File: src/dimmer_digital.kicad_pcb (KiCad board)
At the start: 2 copper layers, 82.5 x 55.9 mm, 28 parts, among them J2 CONECTOR_LEFT, J3 CONNECTOR_SPEED, J4 TERMINAL_AC, J5 TERMINAL_LOAD, J6 CONECTOR_RIGHT, Q1 TIC226, SW1 SWITCH_SPEED, SW2 SW_Push, U1 ATtiny13A-PU, U2 MOC3021M, U3 4N25

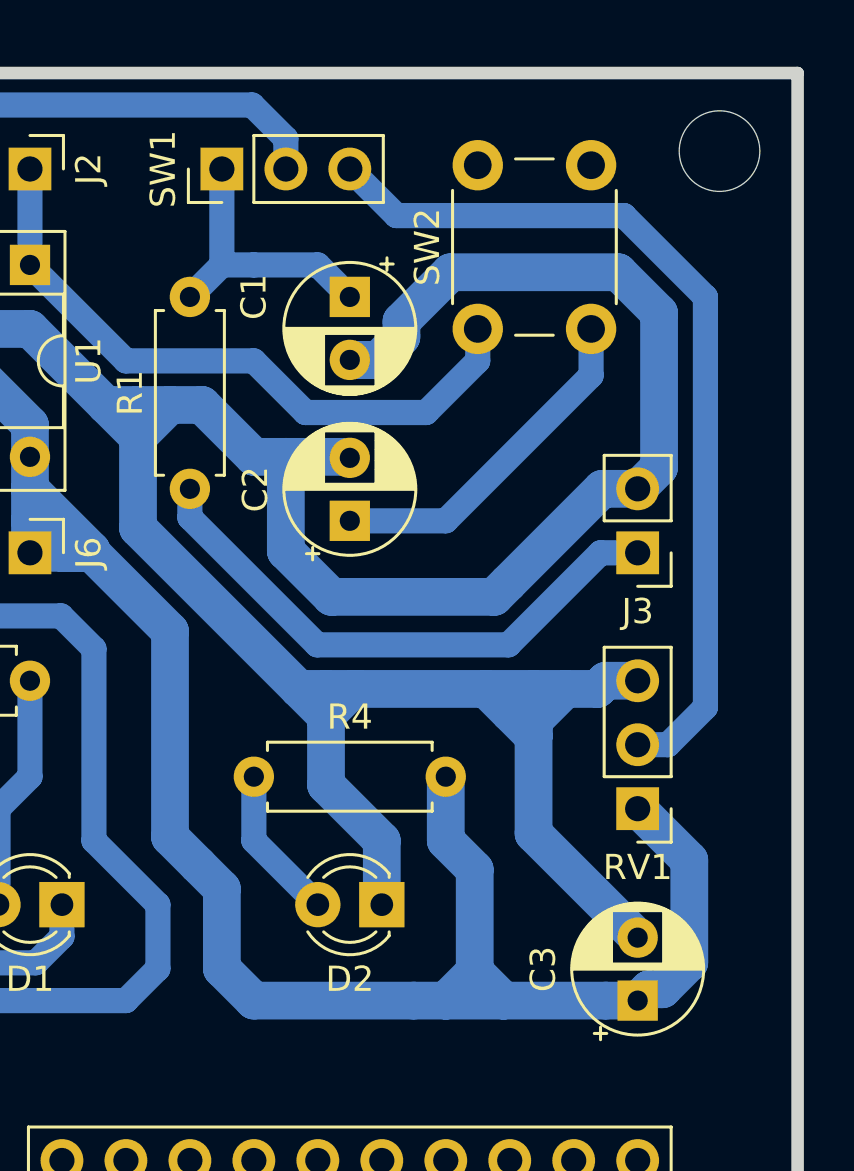
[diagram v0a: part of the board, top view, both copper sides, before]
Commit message: Added pullup to reset pin
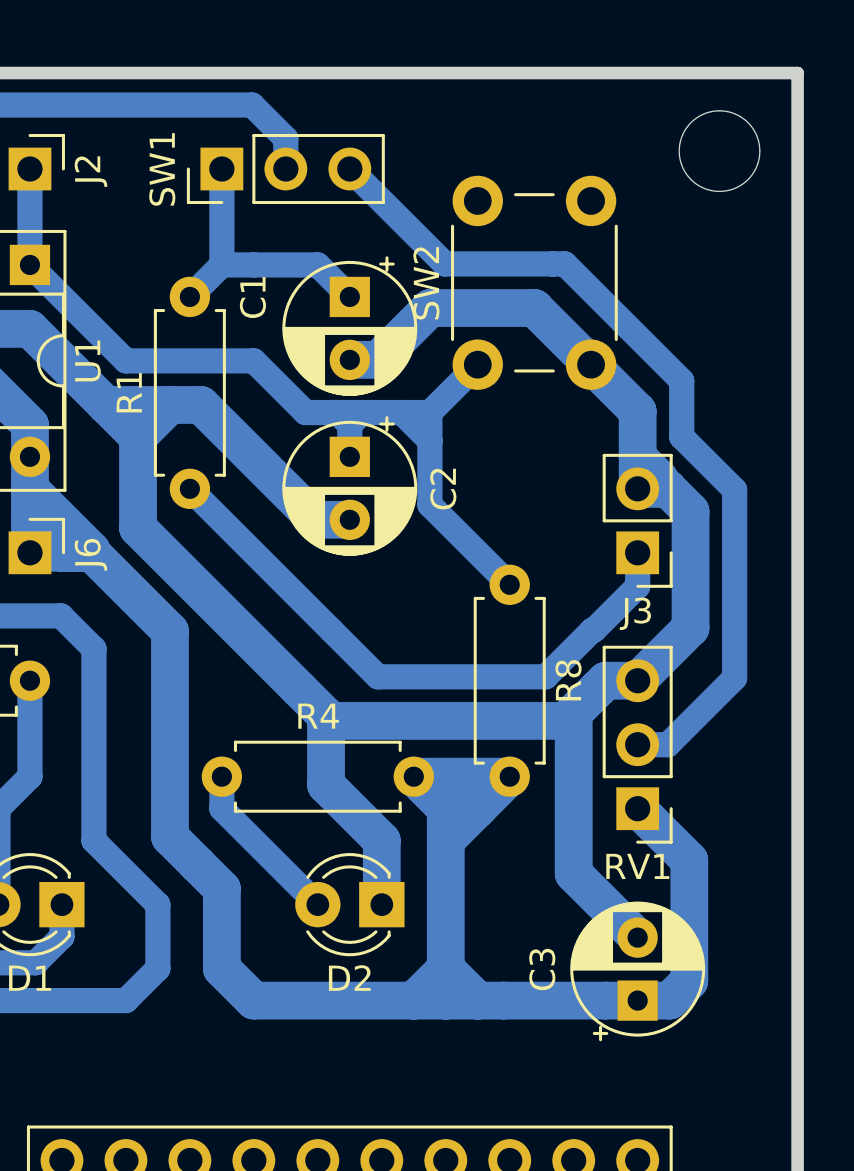
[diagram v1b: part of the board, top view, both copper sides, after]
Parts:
- added R8: 10kΩ, Resistor_THT:R_Axial_DIN0207_L6.3mm_D2.5mm_P7.62mm_Horizontal, F.Cu at (121.9, 45.7)
- R3: value 47kΩ -> 10kΩ
- moved C2 2.54 mm to (115.6, 40.6), turned to 270 degrees
- moved SW2 1.42 mm to (120.7, 37.0)
- moved R4 1.27 mm to (110.5, 53.3)
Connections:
- C2 pad 1: Net-(C2-Pad1) -> RESET
- SW2 pad 2: Net-(C2-Pad1) -> GND
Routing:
- net GND: track 217.2 -> 194.5 mm
- net Net-(C2-Pad1): track 13.8 -> 0.00 mm
- net RESET: track 26.1 -> 37.5 mm
- net +5V: track 109.6 -> 120.3 mm
- net Net-(RV1-Pad2): track 35.8 -> 34.3 mm
- net SPEED_EXTERNAL: track 22.5 -> 23.7 mm
- net Net-(D2-Pad2): track 6.13 -> 6.66 mm

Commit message: Footprint Rev1
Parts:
- removed G***: LOGO, igorkelvin:Logo_Cefet_10mm
- moved R5 17.1 mm to (69.8, 66.0), turned to 0 degrees
- moved Q1 16.1 mm to (71.1, 61.0), turned to 0 degrees
- moved R3 12.6 mm to (102.9, 53.3), turned to 180 degrees
- moved C3 9.16 mm to (119.4, 57.1), turned to 270 degrees
- moved R6 7.73 mm to (69.8, 69.8), turned to 0 degrees
- moved D2 6.35 mm to (110.5, 58.4), turned to 0 degrees
- moved R7 6.35 mm to (69.8, 73.7), turned to 0 degrees
- moved D1 6.35 mm to (97.8, 58.4), turned to 0 degrees
- moved U2 5.68 mm to (91.4, 63.5)
- moved U3 5.24 mm to (83.8, 69.8)
- moved R4 5.08 mm to (115.6, 53.3), turned to 180 degrees
- moved REF** 4.58 mm to (100.3, 68.6)
- moved J4 4.58 mm to (61.0, 61.0)
- moved J5 4.58 mm to (61.0, 73.7)
- moved REF** 4.58 mm to (100.3, 74.9)
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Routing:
- net (no net): track 0.00 -> 58.4 mm
- net LOAD2: track 43.8 -> 13.3 mm
- net Net-(R6-Pad2): track 36.0 -> 6.35 mm
- net Net-(R7-Pad2): track 30.8 -> 6.88 mm
- net +5V: track 120.3 -> 96.5 mm
- net AC1: track 83.3 -> 64.4 mm
- net GND: track 194.5 -> 181.3 mm
- net Net-(D1-Pad1): track 20.4 -> 9.94 mm
- net Net-(Q1-Pad3): track 18.8 -> 8.67 mm
- net AC2: track 87.2 -> 78.7 mm
- net CROSSOVER: track 57.0 -> 49.9 mm
- net Net-(R5-Pad2): track 12.0 -> 7.40 mm
- net Net-(D1-Pad2): track 9.42 -> 10.7 mm
- net Net-(D2-Pad2): track 6.66 -> 6.13 mm
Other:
- outline, holes or cut-outs redrawn
- board text added: "Dimmer c/ ATtiny13 - Rev 1 Igor Kelvin <igorkelvin@gmail.com> 2020-07-20"
- board text removed: "Dimmer c/ ATtiny13 - Rev 0 Igor Kelvin <igorkelvin@gmail.com> 2020-07-11"
